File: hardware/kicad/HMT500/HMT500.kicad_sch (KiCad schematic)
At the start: 0 parts

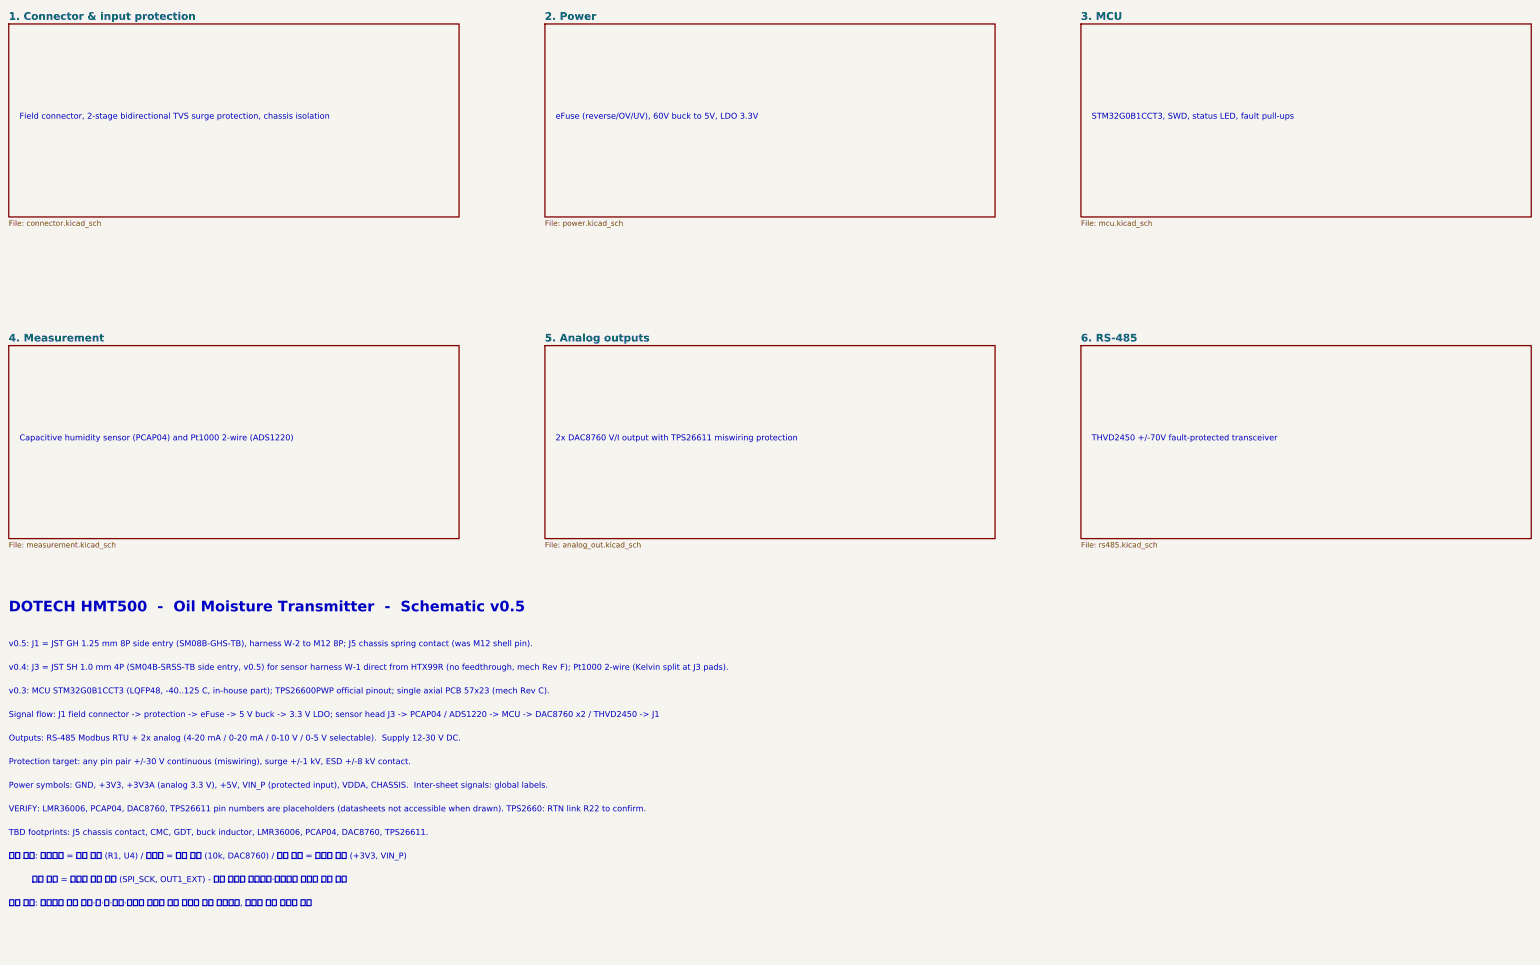
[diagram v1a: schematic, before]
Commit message: Schematic v0.6: parts cleanup (91 -> 75) and PCB temperature sensing
- Removed: fault pull-ups R11-R15 (MCU internal pull-ups), status LED D3/R16
  (not visible after potting), RS-485 R60/R61/D60/D61 (THVD2450 built-in
  protection), VREF+ filter FB2/C19 (MCU ADC only for diagnostics), C11/C2/C6
  (duplicated by adjacent capacitors); VREF+ tied to +3V3 with C20
- PCB temperature with no added parts: ADS1220 internal sensor at the measurement
  front, STM32G0 internal sensor mid-board; compensation plan in circuit-design 5B
- 63 nets, netlist check 0 errors; parts list regenerated; decision log #22/#23

Co-Authored-By: Claude Opus 5.5 <noreply@anthropic.com>
Claude-Session: https://claude.ai/code/session_01JA2o8uJsqp9Vzsg4b665ev
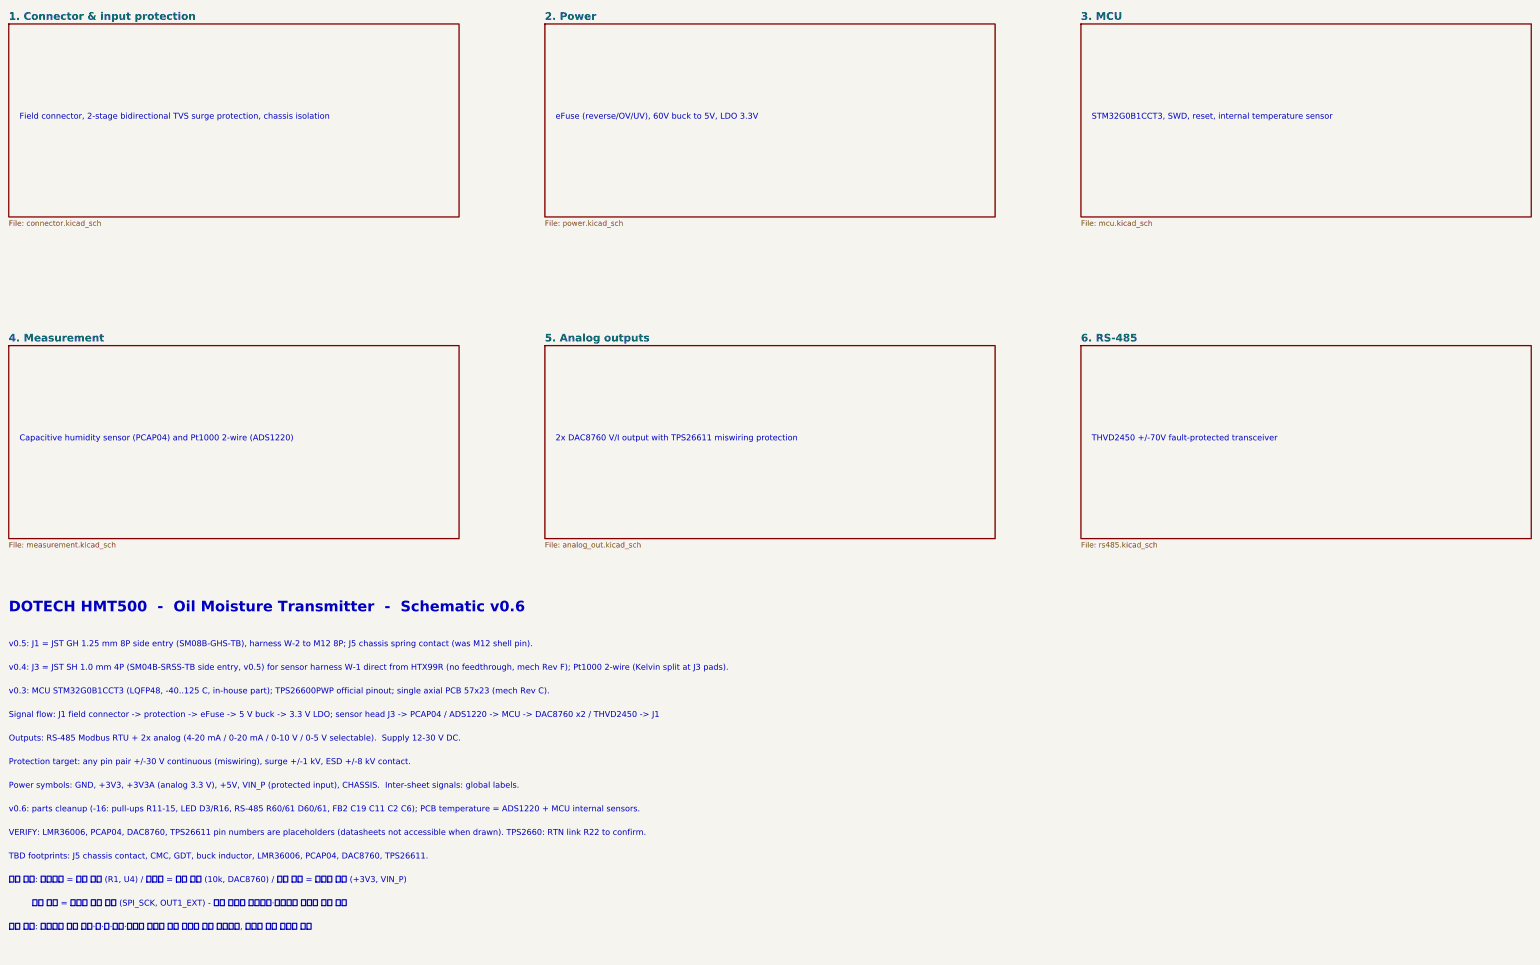
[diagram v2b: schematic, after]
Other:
- note added: "DOTECH HMT500 - Oil Moisture Transmitter - Schematic v0.6"
- note added: "Power symbols: GND, +3V3, +3V3A (analog 3.3 V), +5V, VIN_P (protected input), CHASSIS. Inter-sheet signals: global labels."
- note added: "STM32G0B1CCT3, SWD, reset, internal temperature sensor"
- note added: "v0.6: parts cleanup (-16: pull-ups R11-15, LED D3/R16, RS-485 R60/61 D60/61, FB2 C19 C11 C2 C6); PCB temperature = ADS1220 + MCU internal sensors."
- note removed: "DOTECH HMT500 - Oil Moisture Transmitter - Schematic v0.5"
- note removed: "Power symbols: GND, +3V3, +3V3A (analog 3.3 V), +5V, VIN_P (protected input), VDDA, CHASSIS. Inter-sheet signals: global labels."
- note removed: "STM32G0B1CCT3, SWD, status LED, fault pull-ups"
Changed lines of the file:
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@@
 (kicad_sch (version 20230121) (generator eeschema) (paper "A3")
-(title_block (title "HMT500  Top") (date "2026-09-29") (rev "0.5") (company "DOTECH Co., Ltd.") (comment 1 "Oil moisture transmitter HMT500 - RS-485 + 2x V/I analog output") (comment 2 "Design notes: docs/hw/circuit-design.md") (comment 3 "VERIFY=YES parts: pin numbers LMR36006/PCAP04/DAC8760/TPS26611; TPS2660 R22"))
+(title_block (title "HMT500  Top") (date "2026-09-29") (rev "0.6") (company "DOTECH Co., Ltd.") (comment 1 "Oil moisture transmitter HMT500 - RS-485 + 2x V/I analog output") (comment 2 "Design notes: docs/hw/circuit-design.md") (comment 3 "VERIFY=YES parts: pin numbers LMR36006/PCAP04/DAC8760/TPS26611; TPS2660 R22"))
 (sheet (at 30.48 55.88) (size 106.68 45.72) (fields_autoplaced) (stroke (width 0.1524) (type solid)) (fill (color 0 0 0 0.0000)) (property "Sheetname" "1. Connector & input protection" (at 30.48 55.118 0) (effects (font (size 1.8 1.8) bold) (justify left bottom))) (property "Sheetfile" "connector.kicad_sch" (at 30.48 102.362 0) (effects (font (size 1.27 1.27)) (justify left top))) (instances (project "HMT500" (path "/1ebb025b-11bd-5f7c-aaab-41e2a750e8b3" (page "2")))))
 (text "Field connector, 2-stage bidirectional TVS surge protection, chassis isolation" (at 33.02 78.74 0) (effects (font (size 1.4 1.4)) (justify left bottom)))
@@
 (text "eFuse (reverse/OV/UV), 60V buck to 5V, LDO 3.3V" (at 160.02 78.74 0) (effects (font (size 1.4 1.4)) (justify left bottom)))
 (sheet (at 284.48 55.88) (size 106.68 45.72) (fields_autoplaced) (stroke (width 0.1524) (type solid)) (fill (color 0 0 0 0.0000)) (property "Sheetname" "3. MCU" (at 284.48 55.118 0) (effects (font (size 1.8 1.8) bold) (justify left bottom))) (property "Sheetfile" "mcu.kicad_sch" (at 284.48 102.362 0) (effects (font (size 1.27 1.27)) (justify left top))) (instances (project "HMT500" (path "/1ebb025b-11bd-5f7c-aaab-41e2a750e8b3" (page "4")))))
-(text "STM32G0B1CCT3, SWD, status LED, fault pull-ups" (at 287.02 78.74 0) (effects (font (size 1.4 1.4)) (justify left bottom)))
+(text "STM32G0B1CCT3, SWD, reset, internal temperature sensor" (at 287.02 78.74 0) (effects (font (size 1.4 1.4)) (justify left bottom)))
 (sheet (at 30.48 132.08) (size 106.68 45.72) (fields_autoplaced) (stroke (width 0.1524) (type solid)) (fill (color 0 0 0 0.0000)) (property "Sheetname" "4. Measurement" (at 30.48 131.318 0) (effects (font (size 1.8 1.8) bold) (justify left bottom))) (property "Sheetfile" "measurement.kicad_sch" (at 30.48 178.562 0) (effects (font (size 1.27 1.27)) (justify left top))) (instances (project "HMT500" (path "/1ebb025b-11bd-5f7c-aaab-41e2a750e8b3" (page "5")))))
 (text "Capacitive humidity sensor (PCAP04) and Pt1000 2-wire (ADS1220)" (at 33.02 154.94 0) (effects (font (size 1.4 1.4)) (justify left bottom)))
@@
 (sheet (at 284.48 132.08) (size 106.68 45.72) (fields_autoplaced) (stroke (width 0.1524) (type solid)) (fill (color 0 0 0 0.0000)) (property "Sheetname" "6. RS-485" (at 284.48 131.318 0) (effects (font (size 1.8 1.8) bold) (justify left bottom))) (property "Sheetfile" "rs485.kicad_sch" (at 284.48 178.562 0) (effects (font (size 1.27 1.27)) (justify left top))) (instances (project "HMT500" (path "/1ebb025b-11bd-5f7c-aaab-41e2a750e8b3" (page "7")))))
 (text "THVD2450 +/-70V fault-protected transceiver" (at 287.02 154.94 0) (effects (font (size 1.4 1.4)) (justify left bottom)))
-(text "DOTECH HMT500  -  Oil Moisture Transmitter  -  Schematic v0.5" (at 30.48 195.58 0) (effects (font (size 2.5 2.5) bold) (justify left bottom)))
+(text "DOTECH HMT500  -  Oil Moisture Transmitter  -  Schematic v0.6" (at 30.48 195.58 0) (effects (font (size 2.5 2.5) bold) (justify left bottom)))
 (text "v0.5: J1 = JST GH 1.25 mm 8P side entry (SM08B-GHS-TB), harness W-2 to M12 8P; J5 chassis spring contact (was M12 shell pin)." (at 30.48 203.708 0) (effects (font (size 1.4 1.4)) (justify left bottom)))
 (text "v0.4: J3 = JST SH 1.0 mm 4P (SM04B-SRSS-TB side entry, v0.5) for sensor harness W-1 direct from HTX99R (no feedthrough, mech Rev F); Pt1000 2-wire (Kelvin split at J3 pads)." (at 30.48 209.296 0) (effects (font (size 1.4 1.4)) (justify left bottom)))
@@
 (text "Outputs: RS-485 Modbus RTU + 2x analog (4-20 mA / 0-20 mA / 0-10 V / 0-5 V selectable).  Supply 12-30 V DC." (at 30.48 226.06 0) (effects (font (size 1.4 1.4)) (justify left bottom)))
 (text "Protection target: any pin pair +/-30 V continuous (miswiring), surge +/-1 kV, ESD +/-8 kV contact." (at 30.48 231.648 0) (effects (font (size 1.4 1.4)) (justify left bottom)))
-(text "Power symbols: GND, +3V3, +3V3A (analog 3.3 V), +5V, VIN_P (protected input), VDDA, CHASSIS.  Inter-sheet signals: global labels." (at 30.48 237.236 0) (effects (font (size 1.4 1.4)) (justify left bottom)))
-(text "VERIFY: LMR36006, PCAP04, DAC8760, TPS26611 pin numbers are placeholders (datasheets not accessible when drawn). TPS2660: RTN link R22 to confirm." (at 30.48 242.824 0) (effects (font (size 1.4 1.4)) (justify left bottom)))
-(text "TBD footprints: J5 chassis contact, CMC, GDT, buck inductor, LMR36006, PCAP04, DAC8760, TPS26611." (at 30.48 248.412 0) (effects (font (size 1.4 1.4)) (justify left bottom)))
-(text "표기 규칙: 부품번호 = 굵은 글자 (R1, U4) / 부품값 = 보통 글자 (10k, DAC8760) / 전원 네트 = 기울인 글자 (+3V3, VIN_P)" (at 30.48 254 0) (effects (font (face "NanumGothic") (size 1.4 1.4)) (justify left bottom)))
-(text "         신호 네트 = 테두리 있는 라벨 (SPI_SCK, OUT1_EXT) - 네트 이름은 부품번호·부품명과 겹치지 않게 지음" (at 30.48 259.588 0) (effects (font (face "NanumGothic") (size 1.4 1.4)) (justify left bottom)))
-(text "글자 겹침: 생성기가 부품 몸체·핀·선·라벨·메모와 겹치지 않는 자리에 자동 배치하고, 겹치면 생성 실패로 처리" (at 30.48 265.176 0) (effects (font (face "NanumGothic") (size 1.4 1.4)) (justify left bottom)))
+(text "Power symbols: GND, +3V3, +3V3A (analog 3.3 V), +5V, VIN_P (protected input), CHASSIS.  Inter-sheet signals: global labels." (at 30.48 237.236 0) (effects (font (size 1.4 1.4)) (justify left bottom)))
+(text "v0.6: parts cleanup (-16: pull-ups R11-15, LED D3/R16, RS-485 R60/61 D60/61, FB2 C19 C11 C2 C6); PCB temperature = ADS1220 + MCU internal sensors." (at 30.48 242.824 0) (effects (font (size 1.4 1.4)) (justify left bottom)))
+(text "VERIFY: LMR36006, PCAP04, DAC8760, TPS26611 pin numbers are placeholders (datasheets not accessible when drawn). TPS2660: RTN link R22 to confirm." (at 30.48 248.412 0) (effects (font (size 1.4 1.4)) (justify left bottom)))
+(text "TBD footprints: J5 chassis contact, CMC, GDT, buck inductor, LMR36006, PCAP04, DAC8760, TPS26611." (at 30.48 254 0) (effects (font (size 1.4 1.4)) (justify left bottom)))
+(text "표기 규칙: 부품번호 = 굵은 글자 (R1, U4) / 부품값 = 보통 글자 (10k, DAC8760) / 전원 네트 = 기울인 글자 (+3V3, VIN_P)" (at 30.48 259.588 0) (effects (font (face "NanumGothic") (size 1.4 1.4)) (justify left bottom)))
+(text "         신호 네트 = 테두리 있는 라벨 (SPI_SCK, OUT1_EXT) - 네트 이름은 부품번호·부품명과 겹치지 않게 지음" (at 30.48 265.176 0) (effects (font (face "NanumGothic") (size 1.4 1.4)) (justify left bottom)))
+(text "글자 겹침: 생성기가 부품 몸체·핀·선·라벨·메모와 겹치지 않는 자리에 자동 배치하고, 겹치면 생성 실패로 처리" (at 30.48 270.764 0) (effects (font (face "NanumGothic") (size 1.4 1.4)) (justify left bottom)))
 (sheet_instances (path "/" (page "1")))
 )
